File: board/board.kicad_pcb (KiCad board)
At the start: 4 copper layers, 21 x 78 mm, 44 parts, among them IC1 RTL8305NB-CG, J1 001_I2C, J2 019_100BASE-T_with_CT, J3 019_100BASE-T_with_CT, J4 019_100BASE-T_with_CT, J5 019_100BASE-T_with_CT, J6 019_100BASE-T_with_CT, Y1 25Mhz

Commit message: added decoupling
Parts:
- added C20: 100nF, Capacitor_SMD:C_0603_1608Metric, B.Cu at (154.2, 95.0)
- added C21: 100nF, Capacitor_SMD:C_0603_1608Metric, F.Cu at (153.7, 142.1)
- added C22: 100nF, Capacitor_SMD:C_0603_1608Metric, F.Cu at (153.7, 159.0)
- added C23: 100nF, Capacitor_SMD:C_0603_1608Metric, F.Cu at (157.9, 121.7)
- added C24: 100nF, Capacitor_SMD:C_0603_1608Metric, F.Cu at (152.9, 108.7)
- added C25: 100nF, Capacitor_SMD:C_0603_1608Metric, B.Cu at (154.2, 96.6)
- added C26: 100nF, Capacitor_SMD:C_0603_1608Metric, F.Cu at (153.7, 143.9)
- added C27: 100nF, Capacitor_SMD:C_0603_1608Metric, F.Cu at (153.7, 160.5)
- added C28: 100nF, Capacitor_SMD:C_0603_1608Metric, F.Cu at (157.9, 123.2)
- added C29: 100nF, Capacitor_SMD:C_0603_1608Metric, F.Cu at (152.9, 110.2)
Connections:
- J2 pad 7: unconnected-(J2-Pad7) -> Net-(J2-Pad7)
- J2 pad 8: unconnected-(J2-Pad8) -> Net-(J2-Pad8)
- J3 pad 7: unconnected-(J3-Pad7) -> Net-(J3-Pad7)
- J3 pad 8: unconnected-(J3-Pad8) -> Net-(J3-Pad8)
- J4 pad 7: unconnected-(J4-Pad7) -> Net-(J4-Pad7)
- J4 pad 8: unconnected-(J4-Pad8) -> Net-(J4-Pad8)
- J5 pad 7: unconnected-(J5-Pad7) -> Net-(J5-Pad7)
- J5 pad 8: unconnected-(J5-Pad8) -> Net-(J5-Pad8)
- J6 pad 7: unconnected-(J6-Pad7) -> Net-(J6-Pad7)
- J6 pad 8: unconnected-(J6-Pad8) -> Net-(J6-Pad8)
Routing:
- net Net-(J3-Pad8): track 0.00 -> 9.21 mm, vias 0 -> 1
- net Net-(J3-Pad7): track 0.00 -> 8.07 mm, vias 0 -> 1
- net Net-(J2-Pad8): track 0.00 -> 6.58 mm, vias 0 -> 1
- net Net-(J2-Pad7): track 0.00 -> 5.90 mm, vias 0 -> 1
- net Net-(J4-Pad8): track 0.00 -> 4.66 mm, vias 0 -> 1
- net Net-(J4-Pad7): track 0.00 -> 4.57 mm, vias 0 -> 1
- net Net-(J5-Pad7): track 0.00 -> 4.40 mm, vias 0 -> 1
- net Net-(J5-Pad8): track 0.00 -> 4.36 mm, vias 0 -> 1
- net Net-(J6-Pad8): track 0.00 -> 3.87 mm
- net Net-(J6-Pad7): track 0.00 -> 3.70 mm
- net GND: track 79.0 -> 79.5 mm, vias 64 -> 61

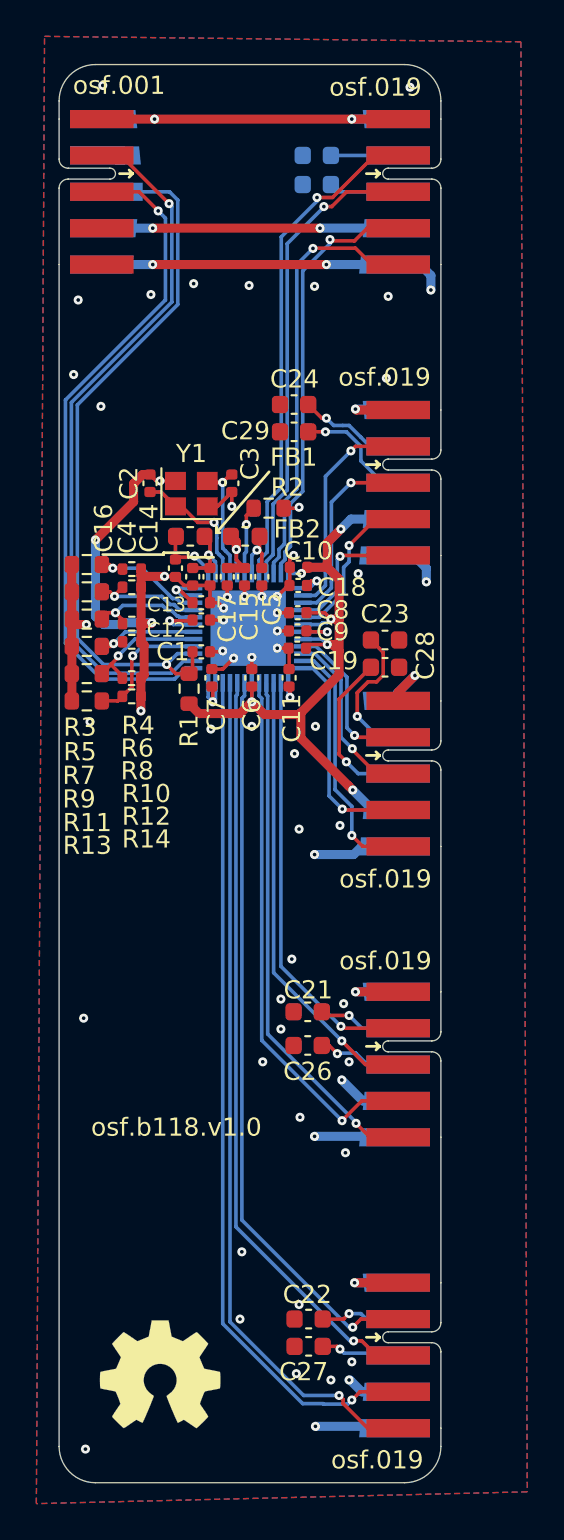
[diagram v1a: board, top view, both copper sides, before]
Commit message: added N filter for 3.3V input
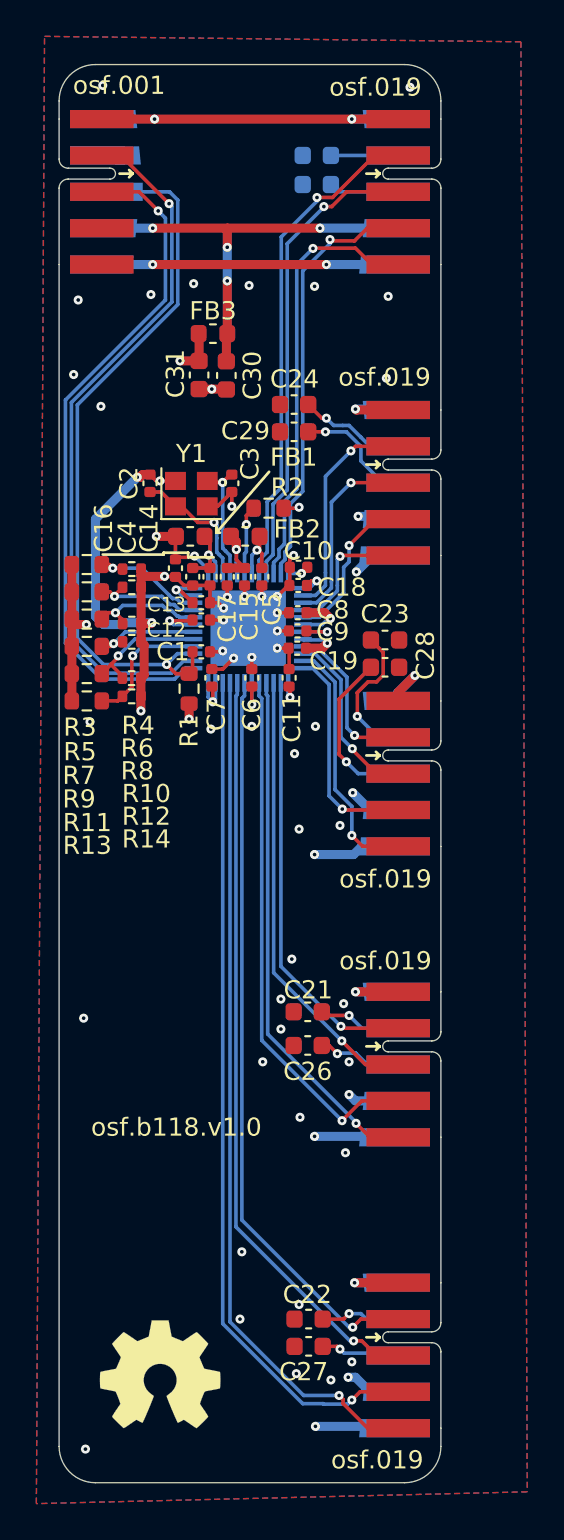
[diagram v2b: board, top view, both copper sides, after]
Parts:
- added C30: 10uF, Capacitor_SMD:C_0603_1608Metric, F.Cu at (149.2, 107.1)
- added C31: 10uF, Capacitor_SMD:C_0603_1608Metric, F.Cu at (147.7, 107.1)
- added FB3: 0R, Inductor_SMD:L_0603_1608Metric, F.Cu at (148.5, 104.8)
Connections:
- C10 pad 1: +3.3V -> /sw_vcc
- C12 pad 1: +3.3V -> /sw_vcc
- C19 pad 1: +3.3V -> /sw_vcc
- C4 pad 1: +3.3V -> /sw_vcc
- C6 pad 1: +3.3V -> /sw_vcc
- C8 pad 1: +3.3V -> /sw_vcc
- FB1 pad 1: +3.3V -> /sw_vcc
- IC1 pad 18: +3.3V -> /sw_vcc
- IC1 pad 31: +3.3V -> /sw_vcc
- IC1 pad 37: +3.3V -> /sw_vcc
- IC1 pad 48: +3.3V -> /sw_vcc
- IC1 pad 6: +3.3V -> /sw_vcc
- IC1 pad 8: +3.3V -> /sw_vcc
- R1 pad 1: +3.3V -> /sw_vcc
- R11 pad 1: +3.3V -> /sw_vcc
- R13 pad 1: +3.3V -> /sw_vcc
- R3 pad 1: +3.3V -> /sw_vcc
- R5 pad 1: +3.3V -> /sw_vcc
- R7 pad 1: +3.3V -> /sw_vcc
- R9 pad 1: +3.3V -> /sw_vcc
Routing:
- net /sw_vcc: track 0.00 -> 54.0 mm, vias 0 -> 10
- net +3.3V: track 146.8 -> 103.4 mm, vias 13 -> 8
- net +5V: track 103.3 -> 98.0 mm, vias 7 -> 6
- net GND: track 79.5 -> 81.1 mm
- added copper zone on In1.Cu, net /sw_vcc
- removed copper zone on In1.Cu, net +3.3V
